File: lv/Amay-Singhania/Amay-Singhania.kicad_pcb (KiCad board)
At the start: 2 copper layers, 4 parts

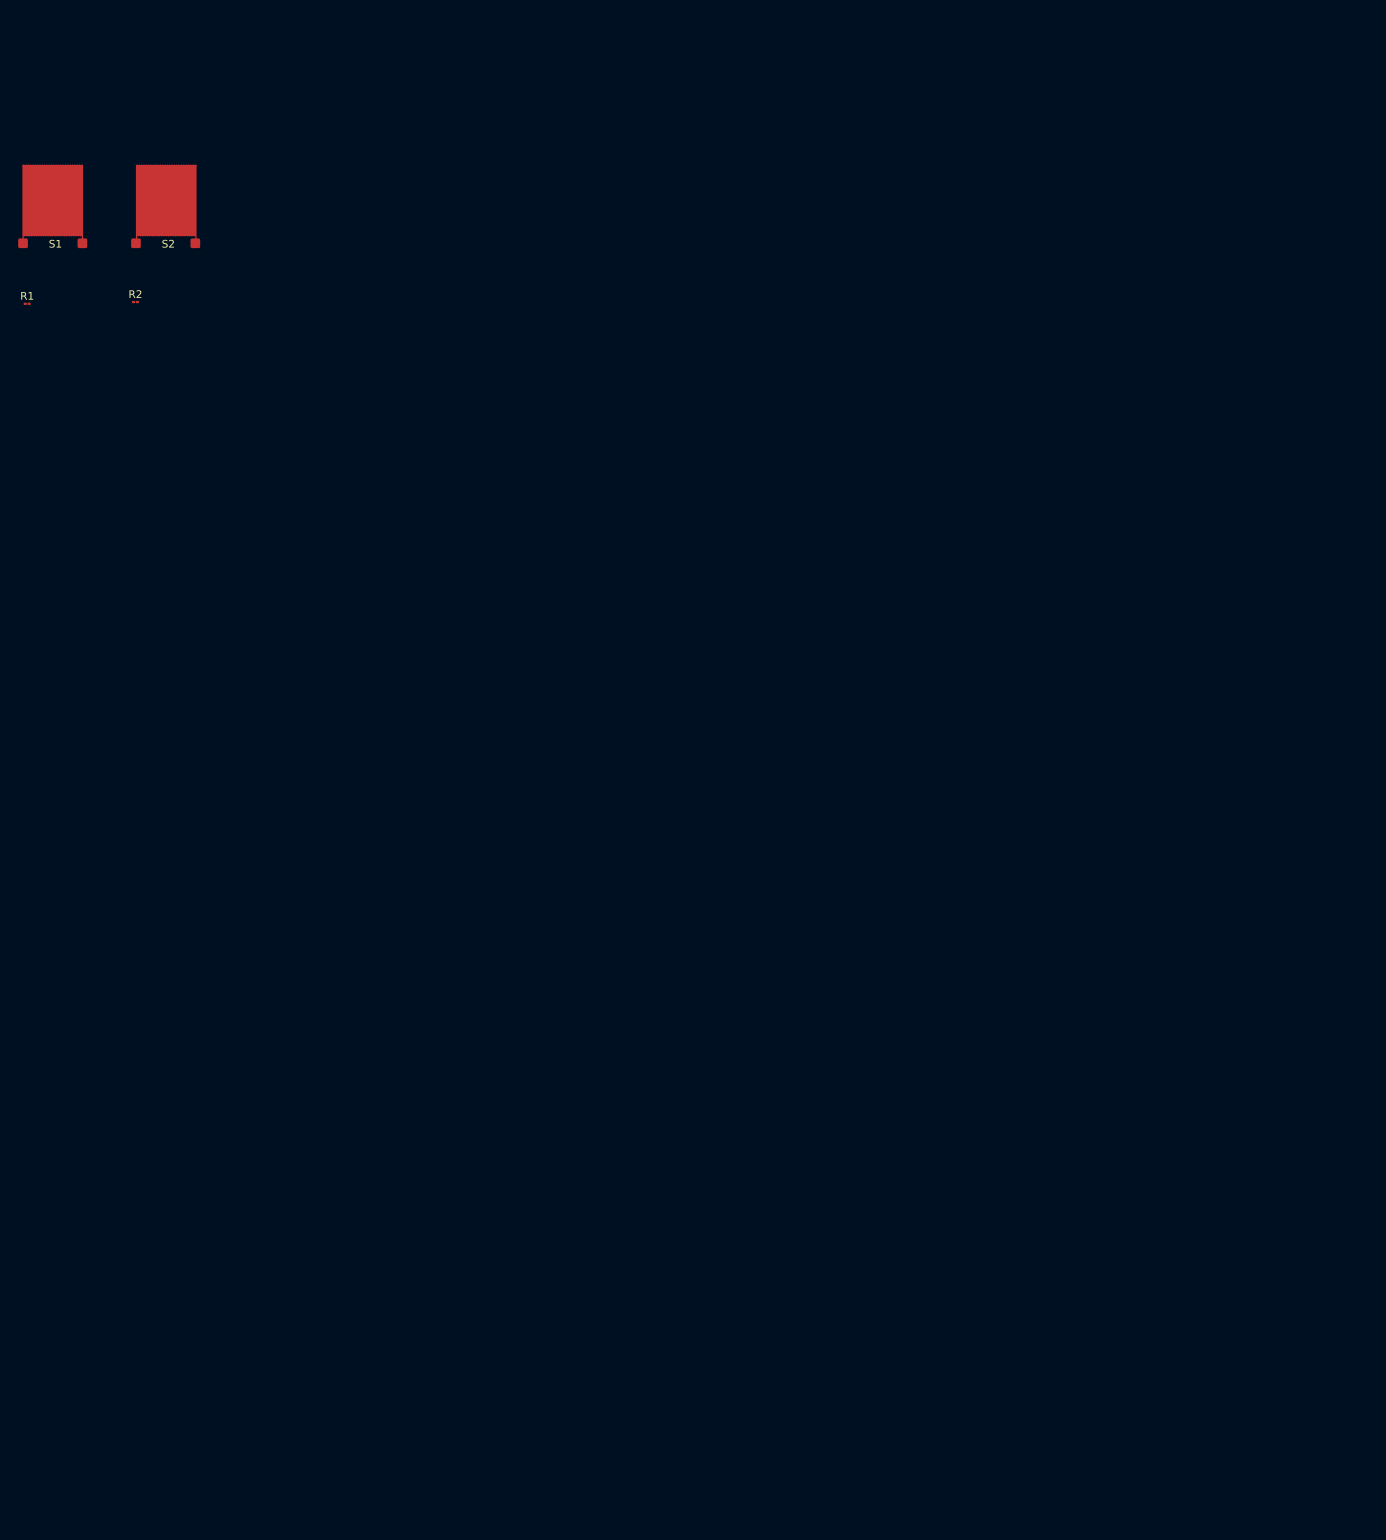
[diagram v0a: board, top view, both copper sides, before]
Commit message: large edits to strain gauge LV onboarding project. gauges made; INAs sourced; 6 channel SPI ADC sourced
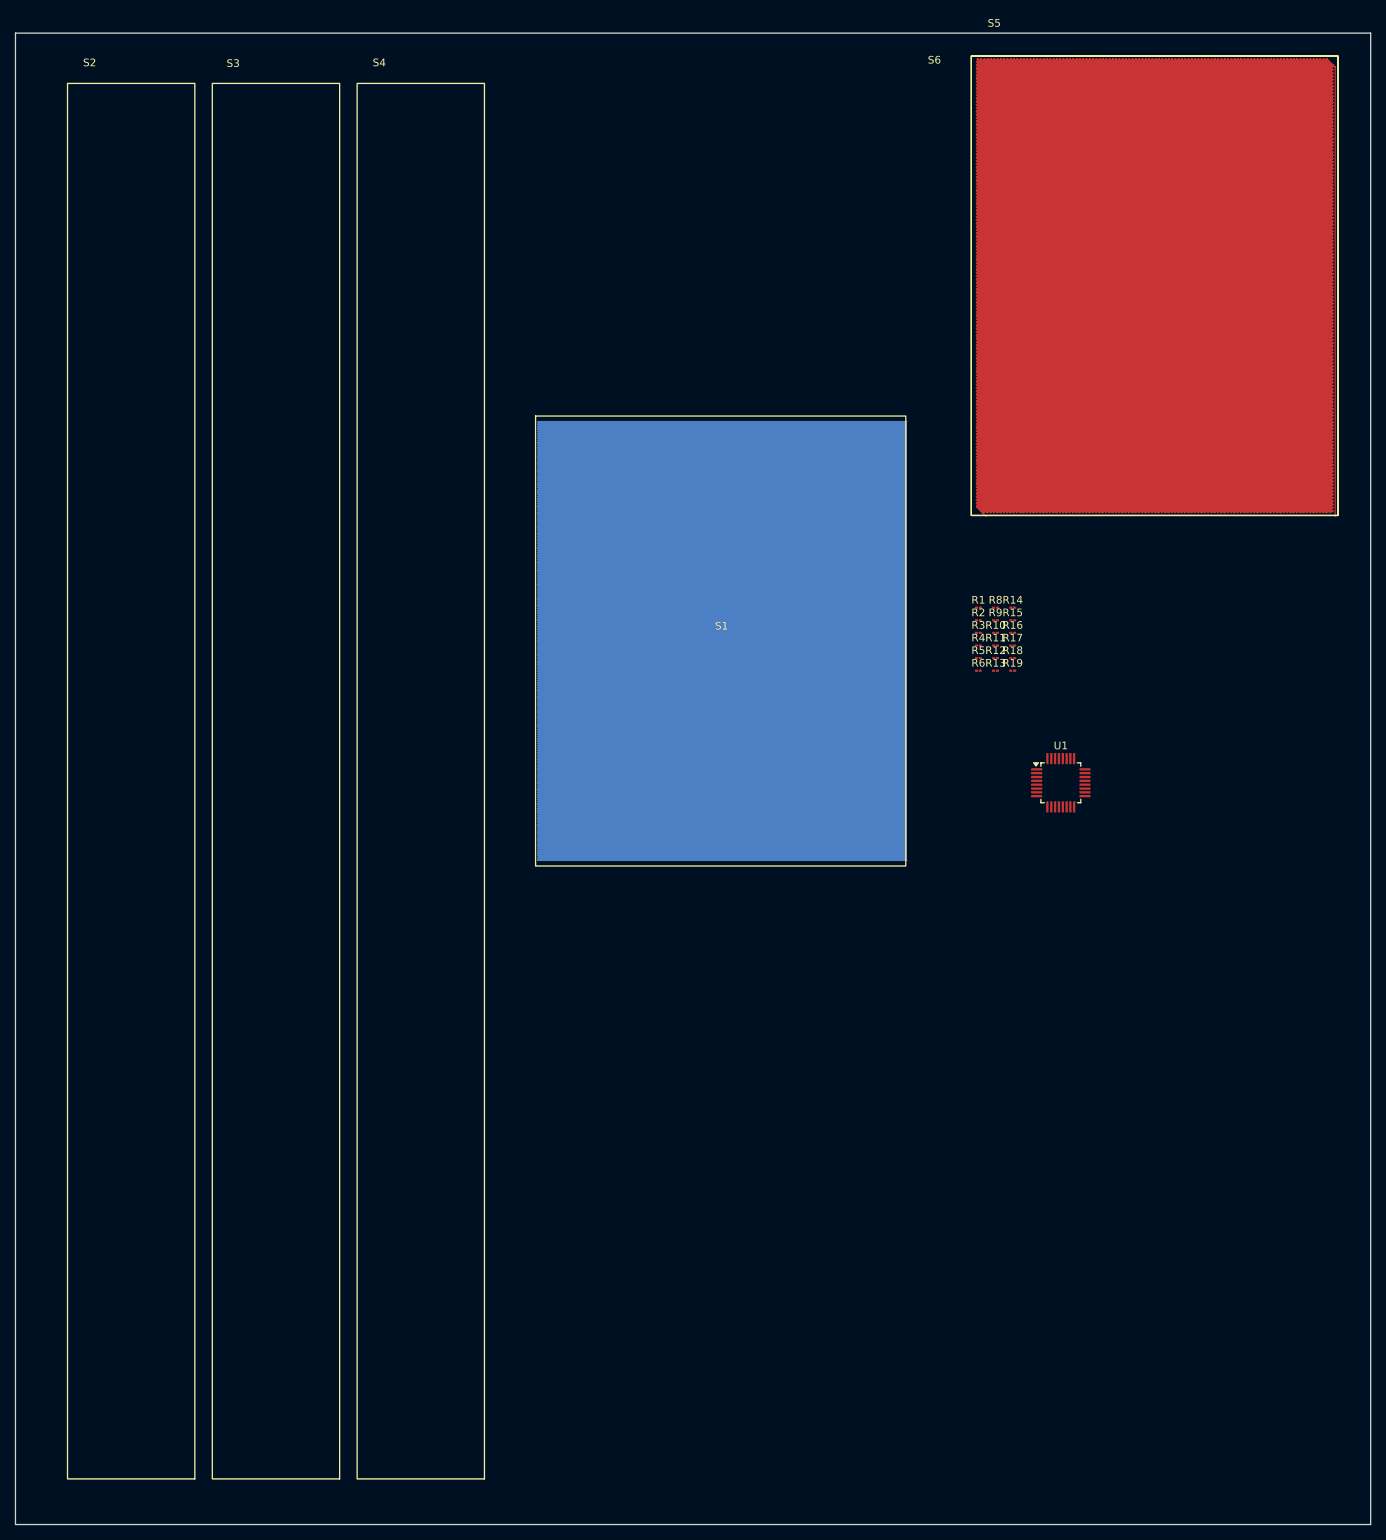
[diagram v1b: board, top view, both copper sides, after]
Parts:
- added R10: 350, Resistor_SMD:R_01005_0402Metric, F.Cu at (143.2, 90.2)
- added R11: 350, Resistor_SMD:R_01005_0402Metric, F.Cu at (143.2, 91.8)
- added R12: 350, Resistor_SMD:R_01005_0402Metric, F.Cu at (143.2, 93.5)
- added R13: 350, Resistor_SMD:R_01005_0402Metric, F.Cu at (143.2, 95.1)
- added R14: 350, Resistor_SMD:R_01005_0402Metric, F.Cu at (145.5, 86.9)
- added R15: 350, Resistor_SMD:R_01005_0402Metric, F.Cu at (145.5, 88.5)
- added R16: 350, Resistor_SMD:R_01005_0402Metric, F.Cu at (145.5, 90.2)
- added R17: 350, Resistor_SMD:R_01005_0402Metric, F.Cu at (145.5, 91.8)
- added R18: 350, Resistor_SMD:R_01005_0402Metric, F.Cu at (145.5, 93.5)
- added R19: 350, Resistor_SMD:R_01005_0402Metric, F.Cu at (145.5, 95.1)
- added R3: 350, Resistor_SMD:R_01005_0402Metric, F.Cu at (141.0, 90.2)
- added R4: 350, Resistor_SMD:R_01005_0402Metric, F.Cu at (141.0, 91.8)
- added R5: 350, Resistor_SMD:R_01005_0402Metric, F.Cu at (141.0, 93.5)
- added R6: 350, Resistor_SMD:R_01005_0402Metric, F.Cu at (141.0, 95.1)
- added R8: 350, Resistor_SMD:R_01005_0402Metric, F.Cu at (143.2, 86.9)
- added R9: 350, Resistor_SMD:R_01005_0402Metric, F.Cu at (143.2, 88.5)
- added S3: StrainGauge, StrainGauge:Strain Gauge V1, F.Cu at (39.7, 17.2)
- added S4: StrainGauge, StrainGauge:Strain Gauge V1, F.Cu at (58.7, 17.2)
- added S5: StrainGauge, StrainGauge:TorsionalGauge-45deg, F.Cu at (139.1, 13.7)
- added S6: StrainGauge, StrainGauge:TorsionalGauge45deg, F.Cu at (139.1, 13.7)
- added U1: ADS127L01xPBS, Package_QFP:TQFP-32_5x5mm_P0.5mm, F.Cu at (151.8, 109.8)
- S1: value StrainGauge -> StrainGaugeRef; footprint StrainGauge:Strain Gauge V1 -> StrainGauge:ReferenceStrainGauge
- S2: value StrainGaugeRef -> StrainGauge
- moved R1 130.7 mm to (141.0, 86.9)
- moved R2 117.9 mm to (141.0, 88.5)
- moved S1 101.1 mm to (107.4, 89.8)
- moved S2 25.9 mm to (20.7, 17.2)
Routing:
- net Net-(R1-Pad1): track 484.7 -> 0.00 mm
- net Net-(R2-Pad1): track 484.7 -> 0.00 mm
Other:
- board outline added: 177.4 x 195.2 mm
- copper layers 2 -> 4

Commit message: wired instrumentation amps and calculated gain measurements
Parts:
- added U2: AD8222HACPZ-R7, AD8222:CP_16_19_ADI, F.Cu at (161.4, 97.5)
- U1: footprint Package_QFP:TQFP-32_5x5mm_P0.5mm -> ADS127L01xPBS:VQFN56_RSH_TEX
